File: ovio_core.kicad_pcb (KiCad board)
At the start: 6 copper layers, 98 x 27.5 mm, 191 parts, among them J101 Conn_01x06, J301 Conn_01x06, J701 USB3_B_Micro, Q501 NTZD3155C, U101 IP4254CZ8-4-TTL, U102 ECP5U_85_CABGA381, U201 TLV62569DRL, U202 TLV62569DRL, U203 TLV62569DRL, U204 TLV62569DRL, U302 W25Q128JVP, U401 MT9V034, U402 MT9V034, U403 KC2016Z50.0000C15XXK, U501 ISM330DHC, U601 MT41J128M16JT-125:K, U701 FT600Q, Y701 30 MHz

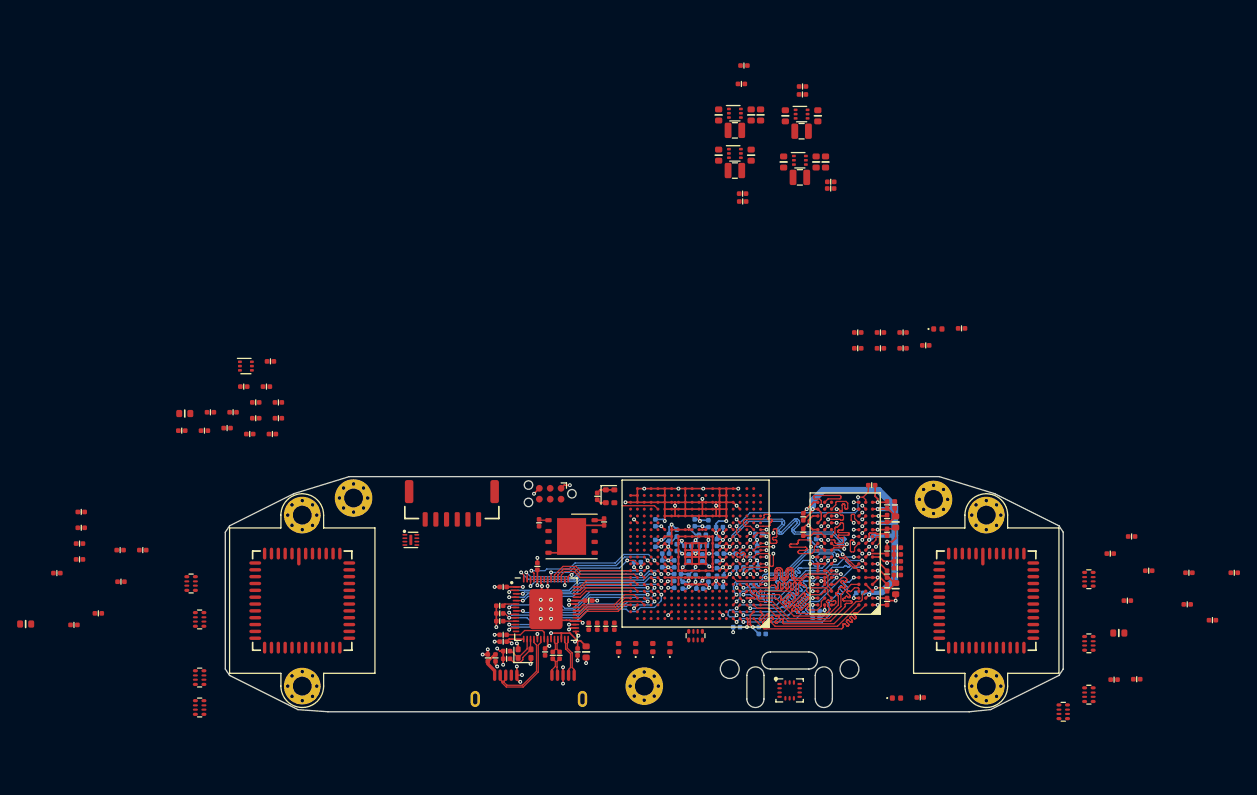
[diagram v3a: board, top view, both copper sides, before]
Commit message: Camera 1, JTAG, SPI Flash routed
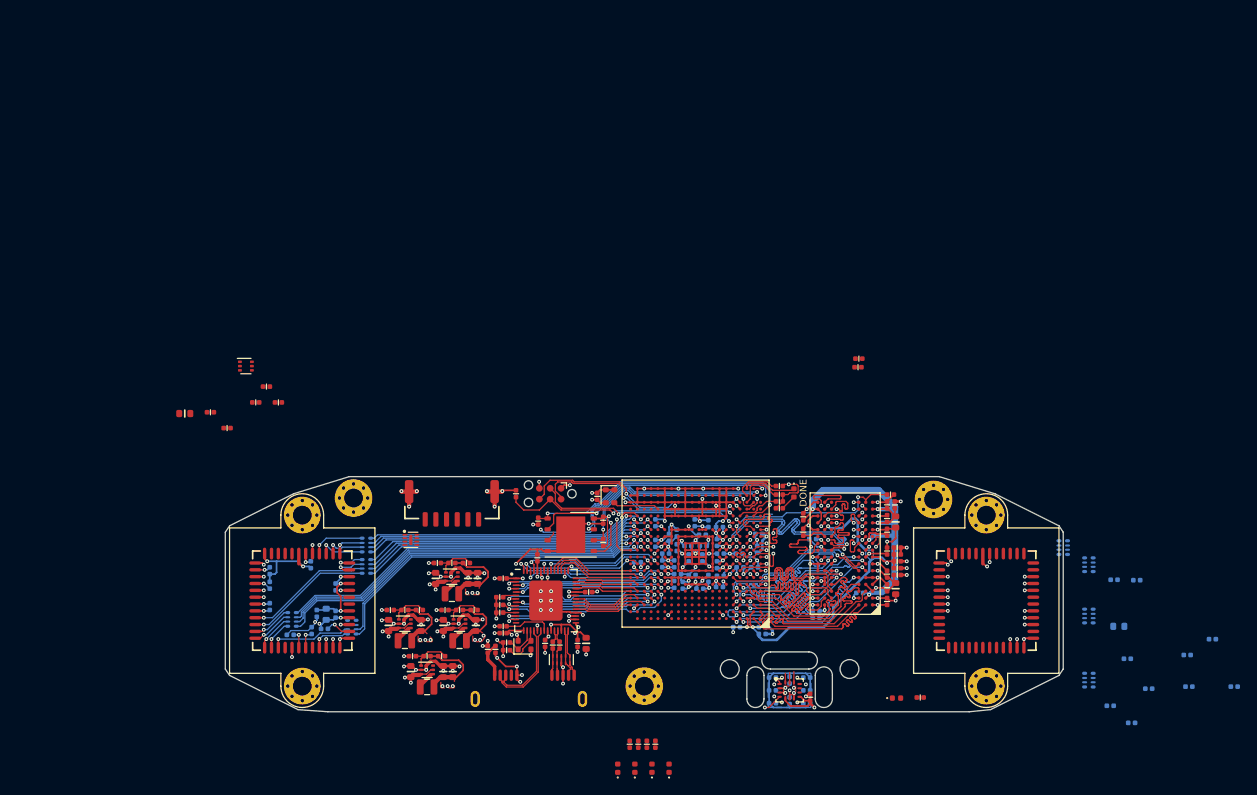
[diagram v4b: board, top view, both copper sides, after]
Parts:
- removed RN405: 22, passive:R_Array_Convex_4x0402
- added C221: 10p, passive:C_0402, F.Cu at (174.5, 97.6)
- added C222: 10p, passive:C_0402, F.Cu at (169.0, 103.1)
- added C223: 10p, passive:C_0402, F.Cu at (175.4, 103.1)
- added C224: 10p, passive:C_0402, F.Cu at (171.6, 108.5)
- added U702: PUSB3FR4Z, dfn:DFN-10-1.0x2.5mm_P0.5mm, F.Cu at (187.3, 108.9)
- C401, C402, C403, C404, C405, C406, C407, C408, C409, C410, FB401, FB402, R401, R402, R403, R404, R405, R406, R407, R408, R409, R410, R504, R505, R506, R507, R509, R510, R511, R512, RN401, RN402, RN403, RN404, RN406, RN407, RN408, RN409: moved to B.Cu
- C710, C711: value 11p -> 10p
- moved R204 77.2 mm to (167.3, 103.1)
- moved R203 75.9 mm to (170.7, 103.1), turned to 180 degrees
- moved C204 75.5 mm to (167.1, 104.9)
- moved C206 75.5 mm to (170.9, 104.9)
- moved L202 75.5 mm to (169.0, 106.7)
- moved U202 75.5 mm to (169.0, 104.7)
- moved R509 75.5 mm to (212.0, 112.5)
- moved R208 74.0 mm to (169.9, 108.5)
- moved C201 73.8 mm to (169.7, 110.3)
- moved C208 73.8 mm to (174.6, 110.3)
- moved C220 73.8 mm to (173.5, 110.3)
- moved L204 73.8 mm to (171.6, 112.1)
- moved U204 73.8 mm to (171.6, 110.1)
- moved R507 73.7 mm to (214.0, 113.7), turned to 90 degrees
- moved R506 72.8 mm to (216.0, 111.0), turned to 180 degrees
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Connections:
- net Net-(Q501-Pad2) renamed /Heated IMU/HEATER_BASE
- net Net-(R302-Pad2) renamed /FPGA Config/CFG_1
- RN406 pad 1: /2x cameras/CAM1_FLASH -> Net-(RN406-Pad1)
- RN406 pad 2: /2x cameras/CAM1_PIXCLK -> Net-(RN406-Pad2)
- RN406 pad 4: /2x cameras/CAM1_LV -> /2x cameras/CAM1_FLASH
- RN406 pad 5: /2x cameras/CAM1_LV_P -> /2x cameras/CAM1_FLASH_P
- RN406 pad 7: /2x cameras/CAM1_PIXCLK_P -> Net-(RN406-Pad7)
- RN406 pad 8: /2x cameras/CAM1_FLASH_P -> Net-(RN406-Pad8)
- RN407 pad 4: /2x cameras/CAM1_D3_P -> /2x cameras/CAM1_PIXCLK_P
- RN407 pad 5: /2x cameras/CAM1_D3 -> /2x cameras/CAM1_PIXCLK
- RN408 pad 1: /2x cameras/CAM1_D4_P -> /2x cameras/CAM1_D6_P
- RN408 pad 3: /2x cameras/CAM1_D6_P -> /2x cameras/CAM1_D4_P
- RN408 pad 4: /2x cameras/CAM1_D7_P -> /2x cameras/CAM1_D3_P
- RN408 pad 5: /2x cameras/CAM1_D7 -> /2x cameras/CAM1_D3
- RN408 pad 6: /2x cameras/CAM1_D6 -> /2x cameras/CAM1_D4
- RN408 pad 8: /2x cameras/CAM1_D4 -> /2x cameras/CAM1_D6
- RN409 pad 1: /2x cameras/CAM1_D8_P -> /2x cameras/CAM1_LV_P
- RN409 pad 3: Net-(RN409-Pad3) -> /2x cameras/CAM1_D8_P
- RN409 pad 4: Net-(RN409-Pad4) -> /2x cameras/CAM1_D7_P
- RN409 pad 5: Net-(RN409-Pad5) -> /2x cameras/CAM1_D7
- RN409 pad 6: Net-(RN409-Pad6) -> /2x cameras/CAM1_D8
- RN409 pad 8: /2x cameras/CAM1_D8 -> /2x cameras/CAM1_LV
- U102 pad L16: /2x cameras/CAM1_D0 -> /2x cameras/CAM1_TRIGGER
- U102 pad L17: /2x cameras/CAM1_D1 -> /2x cameras/CAM1_RESET
- U102 pad L18: /2x cameras/CAM1_D2 -> /2x cameras/CAM1_SCLK
- U102 pad M17: /2x cameras/CAM1_D5 -> /2x cameras/CAM1_SDATA
- U102 pad M18: /2x cameras/CAM1_D3 -> /2x cameras/CAM1_FLASH
- U102 pad M20: /2x cameras/CAM1_FLASH -> /2x cameras/CAM1_D9
- U102 pad N16: /2x cameras/CAM1_D4 -> Net-(U102-PadN16)
- U102 pad N17: /2x cameras/CAM1_D8 -> /2x cameras/CAM1_SYSCLK
- U102 pad N18: /2x cameras/CAM1_D6 -> /2x cameras/CAM1_D8
- U102 pad N19: /2x cameras/CAM1_SDATA -> /2x cameras/CAM1_D6
- U102 pad N20: /2x cameras/CAM1_SCLK -> /2x cameras/CAM1_D7
- U102 pad P16: /2x cameras/CAM1_D9 -> Net-(U102-PadP16)
- U102 pad P17: /2x cameras/CAM1_D7 -> /2x cameras/CAM1_D5
- U102 pad P19: /2x cameras/CAM1_RESET -> /2x cameras/CAM1_D4
- U102 pad R16: /2x cameras/CAM1_TRIGGER -> Net-(U102-PadR16)
- U102 pad R17: /2x cameras/CAM1_SYSCLK -> /2x cameras/CAM1_D3
- U102 pad T18: Net-(U102-PadT18) -> /2x cameras/CAM1_D0
- U102 pad T19: Net-(U102-PadT19) -> /2x cameras/CAM1_D2
- U102 pad T20: Net-(U102-PadT20) -> /2x cameras/CAM1_D1
- U401 pad 23: /2x cameras/CAM0_TRIGGER_P -> /2x cameras/CAM0_TRIGGER
- U401 pad 47: /2x cameras/CAM0_SYSCLK_P -> /2x cameras/CAM0_SYSCLK
- U402 pad 23: /2x cameras/CAM1_TRIGGER_P -> /2x cameras/CAM1_TRIGGER
- U402 pad 47: /2x cameras/CAM1_SYSCLK_P -> /2x cameras/CAM1_SYSCLK
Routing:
- net GND: track 235.8 -> 330.5 mm, vias 85 -> 159
- net +1V5: track 18.2 -> 107.8 mm, vias 9 -> 15
- net /2x cameras/CAM1_TRIGGER: track 0.00 -> 54.2 mm, vias 0 -> 2
- net +3V3: track 40.0 -> 93.7 mm, vias 18 -> 34
- net /2x cameras/CAM1_SDATA: track 0.00 -> 52.1 mm, vias 0 -> 2
- net /2x cameras/CAM1_SCLK: track 0.00 -> 51.3 mm, vias 0 -> 2
- net /2x cameras/CAM1_RESET: track 0.00 -> 48.8 mm, vias 0 -> 2
- net /2x cameras/CAM1_D8: track 0.00 -> 45.2 mm, vias 0 -> 1
- net /2x cameras/CAM1_LV: track 0.00 -> 45.0 mm, vias 0 -> 1
- net +2V5: track 4.96 -> 49.8 mm, vias 4 -> 7
- net +5V: track 1.82 -> 46.5 mm, vias 3 -> 11
- net /DDR3 Memory/VREF: track 11.7 -> 55.7 mm
- net /2x cameras/CAM1_D9: track 0.00 -> 43.3 mm, vias 0 -> 1
- net /2x cameras/CAM1_D7: track 0.00 -> 42.8 mm, vias 0 -> 1
- net /2x cameras/CAM1_SYSCLK: track 0.00 -> 41.9 mm, vias 0 -> 2
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- added copper zone on F.Cu, net +1V1
- added copper zone on GND_PWR2, net +1V1
- added copper zone on F.Cu, net +1V5
- added copper zone on F.Cu, net +2V5
- added copper zone on F.Cu, net +3V3
- added copper zone on GND_PWR2, net +3V3
- added copper zone on B.Cu, net GND
- added copper zone on F.Cu, net GND
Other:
- board text added: "DONE"

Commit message: DRC pass, routing finished
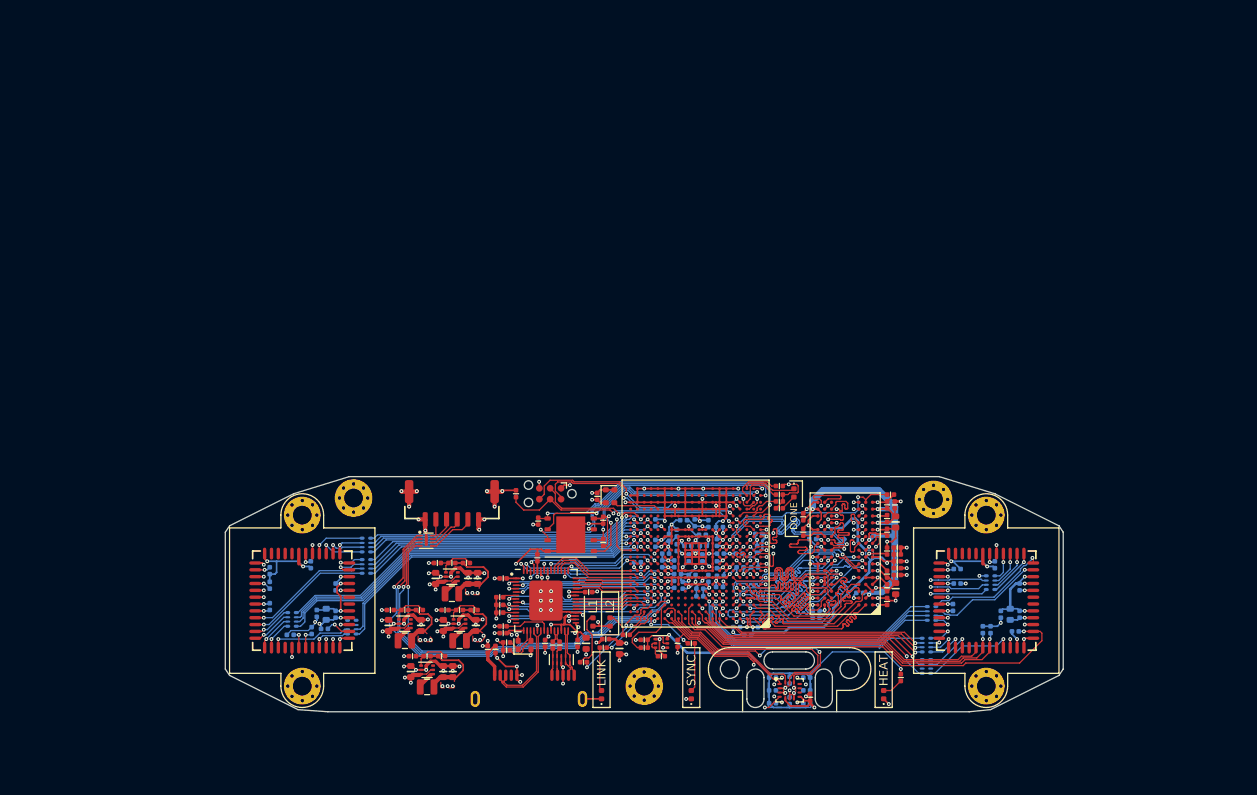
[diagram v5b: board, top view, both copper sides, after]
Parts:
- C301, C302: moved to B.Cu
- moved R508 61.0 mm to (200.9, 107.0), turned to 270 degrees
- moved Q501 58.4 mm to (199.0, 107.0)
- moved C501 57.8 mm to (194.1, 107.6), turned to 270 degrees
- moved R503 55.9 mm to (199.0, 108.5), turned to 180 degrees
- moved R502 54.7 mm to (197.0, 106.6), turned to 180 degrees
- moved R501 53.7 mm to (197.0, 107.5), turned to 180 degrees
- moved FB501 47.2 mm to (192.5, 106.5), turned to 180 degrees
- moved C302 33.4 mm to (203.5, 101.5), turned to 180 degrees
- moved R407 27.2 mm to (233.6, 98.3), turned to 180 degrees
- moved C301 27.1 mm to (201.6, 92.6), turned to 180 degrees
- moved R401 26.9 mm to (236.6, 105.4), turned to 90 degrees
- moved C408 26.5 mm to (240.9, 103.6), turned to 270 degrees
- moved C407 24.8 mm to (233.1, 102.8), turned to 90 degrees
- moved R405 23.2 mm to (237.5, 105.4), turned to 90 degrees
- moved R409 22.9 mm to (233.6, 100.0), turned to 180 degrees
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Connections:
- J101 pad 3: /USER_GPIO0 -> /USER_GPIO2
- J101 pad 5: /USER_GPIO2 -> /USER_GPIO0
- RN401 pad 2: /2x cameras/CAM0_PIXCLK -> Net-(RN401-Pad2)
- RN401 pad 3: /2x cameras/CAM0_FV_P -> /2x cameras/CAM0_FV
- RN401 pad 4: /2x cameras/CAM0_LV_P -> Net-(RN401-Pad4)
- RN401 pad 5: /2x cameras/CAM0_LV_P -> Net-(RN401-Pad5)
- RN401 pad 7: /2x cameras/CAM0_PIXCLK_P -> Net-(RN401-Pad7)
- RN402 pad 1: /2x cameras/CAM0_D0_P -> /2x cameras/CAM0_PIXCLK_P
- RN402 pad 2: /2x cameras/CAM0_D1_P -> /2x cameras/CAM0_D0_P
- RN402 pad 3: /2x cameras/CAM0_D2_P -> /2x cameras/CAM0_D1_P
- RN402 pad 4: /2x cameras/CAM0_D3_P -> /2x cameras/CAM0_D2_P
- RN402 pad 5: /2x cameras/CAM0_D3 -> /2x cameras/CAM0_D2
- RN402 pad 6: /2x cameras/CAM0_D2 -> /2x cameras/CAM0_D1
- RN402 pad 7: /2x cameras/CAM0_D1 -> /2x cameras/CAM0_D0
- RN402 pad 8: /2x cameras/CAM0_D0 -> /2x cameras/CAM0_PIXCLK
- RN403 pad 1: /2x cameras/CAM0_D4_P -> /2x cameras/CAM0_D3_P
- RN403 pad 2: /2x cameras/CAM0_D5_P -> /2x cameras/CAM0_D4_P
- RN403 pad 3: /2x cameras/CAM0_D6_P -> /2x cameras/CAM0_D5_P
- RN403 pad 4: /2x cameras/CAM0_D7_P -> /2x cameras/CAM0_D6_P
- RN403 pad 5: /2x cameras/CAM0_D7 -> /2x cameras/CAM0_D6
- RN403 pad 6: /2x cameras/CAM0_D6 -> /2x cameras/CAM0_D5
- RN403 pad 7: /2x cameras/CAM0_D5 -> /2x cameras/CAM0_D4
- RN403 pad 8: /2x cameras/CAM0_D4 -> /2x cameras/CAM0_D3
- RN404 pad 1: /2x cameras/CAM0_D8_P -> /2x cameras/CAM0_D7_P
- RN404 pad 2: /2x cameras/CAM0_D9_P -> /2x cameras/CAM0_D8_P
- RN404 pad 3: Net-(RN404-Pad3) -> /2x cameras/CAM0_D9_P
- RN404 pad 4: Net-(RN404-Pad4) -> /2x cameras/CAM0_LV_P
- RN404 pad 5: Net-(RN404-Pad5) -> /2x cameras/CAM0_LV
- RN404 pad 6: Net-(RN404-Pad6) -> /2x cameras/CAM0_D9
- RN404 pad 7: /2x cameras/CAM0_D9 -> /2x cameras/CAM0_D8
- RN404 pad 8: /2x cameras/CAM0_D8 -> /2x cameras/CAM0_D7
- U101 pad 1: /P_USER_GPIO2 -> /P_USER_GPIO0
- U101 pad 3: /P_USER_GPIO0 -> /P_USER_GPIO2
- U101 pad 6: /USER_GPIO0 -> /USER_GPIO2
- U101 pad 8: /USER_GPIO2 -> /USER_GPIO0
- U102 pad A11: Net-(U102-PadA11) -> /2x cameras/CAM0_SCLK
- U102 pad A13: Net-(U102-PadA13) -> /IMU_CS
- U102 pad A14: /IMU_SDI -> /IMU_SDO
- U102 pad A15: Net-(U102-PadA15) -> /IMU_INT
- U102 pad A6: /2x cameras/CAM0_FLASH -> Net-(U102-PadA6)
- U102 pad A7: /2x cameras/CAM0_D9 -> /2x cameras/CAM0_D8
- U102 pad A8: /2x cameras/CAM0_TRIGGER -> /2x cameras/CAM0_LV
- U102 pad A9: Net-(U102-PadA9) -> /2x cameras/CAM0_FLASH
- U102 pad B10: Net-(U102-PadB10) -> /2x cameras/CAM0_TRIGGER
- U102 pad B11: Net-(U102-PadB11) -> /2x cameras/CAM0_SDATA
- U102 pad B13: Net-(U102-PadB13) -> /IMU_SCK
- U102 pad B15: /IMU_INT -> /IMU_SDI
- U102 pad B6: /2x cameras/CAM0_FV_P -> Net-(U102-PadB6)
- U102 pad B8: /2x cameras/CAM0_D8 -> /2x cameras/CAM0_D9
- U102 pad B9: /2x cameras/CAM0_SDATA -> /2x cameras/CAM0_FV
- U102 pad C10: /2x cameras/CAM0_SCLK -> /2x cameras/CAM0_D2
- U102 pad C11: Net-(U102-PadC11) -> /2x cameras/CAM0_RESET
- U102 pad C14: /IMU_SCK -> Net-(U102-PadC14)
- U102 pad C6: /2x cameras/CAM0_D3 -> Net-(U102-PadC6)
- U102 pad C7: /2x cameras/CAM0_D4 -> /2x cameras/CAM0_D3
- U102 pad C8: /2x cameras/CAM0_D7 -> /2x cameras/CAM0_D4
- U102 pad D14: /IMU_CS -> Net-(U102-PadD14)
- U102 pad D6: /2x cameras/CAM0_D0 -> Net-(U102-PadD6)
- U102 pad D7: /2x cameras/CAM0_D2 -> /2x cameras/CAM0_D5
- U102 pad D9: /2x cameras/CAM0_SYSCLK -> /2x cameras/CAM0_D7
- U102 pad E14: /IMU_SDO -> Net-(U102-PadE14)
- U102 pad E6: /2x cameras/CAM0_LV_P -> Net-(U102-PadE6)
- U102 pad E7: /2x cameras/CAM0_D1 -> /2x cameras/CAM0_SYSCLK
- U102 pad E8: /2x cameras/CAM0_D5 -> /2x cameras/CAM0_D0
- U102 pad E9: /2x cameras/CAM0_RESET -> /2x cameras/CAM0_D1
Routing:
- net /2x cameras/CAM0_RESET: track 0.00 -> 50.6 mm, vias 0 -> 1
- net /P_USER_GPIO2: track 0.00 -> 48.0 mm, vias 0 -> 2
- net /P_USER_GPIO0: track 0.00 -> 47.2 mm, vias 0 -> 2
- net /P_USER_FLASH_OUT: track 0.00 -> 46.3 mm, vias 0 -> 2
- net /P_USER_GPIO1: track 0.00 -> 45.8 mm, vias 0 -> 2
- net /2x cameras/CAM0_SYSCLK: track 0.00 -> 42.6 mm, vias 0 -> 2
- net /2x cameras/CAM0_D1: track 0.00 -> 40.3 mm, vias 0 -> 2
- net /2x cameras/CAM0_PIXCLK: track 0.00 -> 40.2 mm, vias 0 -> 2
- net /2x cameras/CAM0_SCLK: track 0.00 -> 40.0 mm, vias 0 -> 1
- net +5V: track 46.5 -> 86.4 mm, vias 11 -> 14
- net /2x cameras/CAM0_SDATA: track 0.00 -> 39.7 mm, vias 0 -> 1
- net /2x cameras/CAM0_D0: track 0.00 -> 39.3 mm, vias 0 -> 2
- net /2x cameras/CAM0_D2: track 0.00 -> 38.0 mm, vias 0 -> 2
- net /2x cameras/CAM0_TRIGGER: track 0.00 -> 35.9 mm
- net /2x cameras/CAM0_D5: track 0.00 -> 31.3 mm, vias 0 -> 1
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- added copper zone on GND_PWR3, net +1V5
- added copper zone on GND_PWR2, net +2V5
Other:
- outline, holes or cut-outs redrawn
- board text added: "By Emil Fresk (@korken89)"
- board text added: "HEAT"
- board text added: "L1"
- board text added: "L2"
- board text added: "LINK"
- board text added: "OVIO Core"
- board text added: "SYNC"
